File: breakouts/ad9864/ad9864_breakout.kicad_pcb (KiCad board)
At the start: 2 copper layers, 82 parts, among them P101 CONN_01X02, P102 CONN_01X08, P103 CONN_02X08, U101 CONN_SMA, U102 CONN_SMA, U103 ad9864, U104 TXCO, U105 CONN_SMA, U106 CONN_SMA, U107 max2605

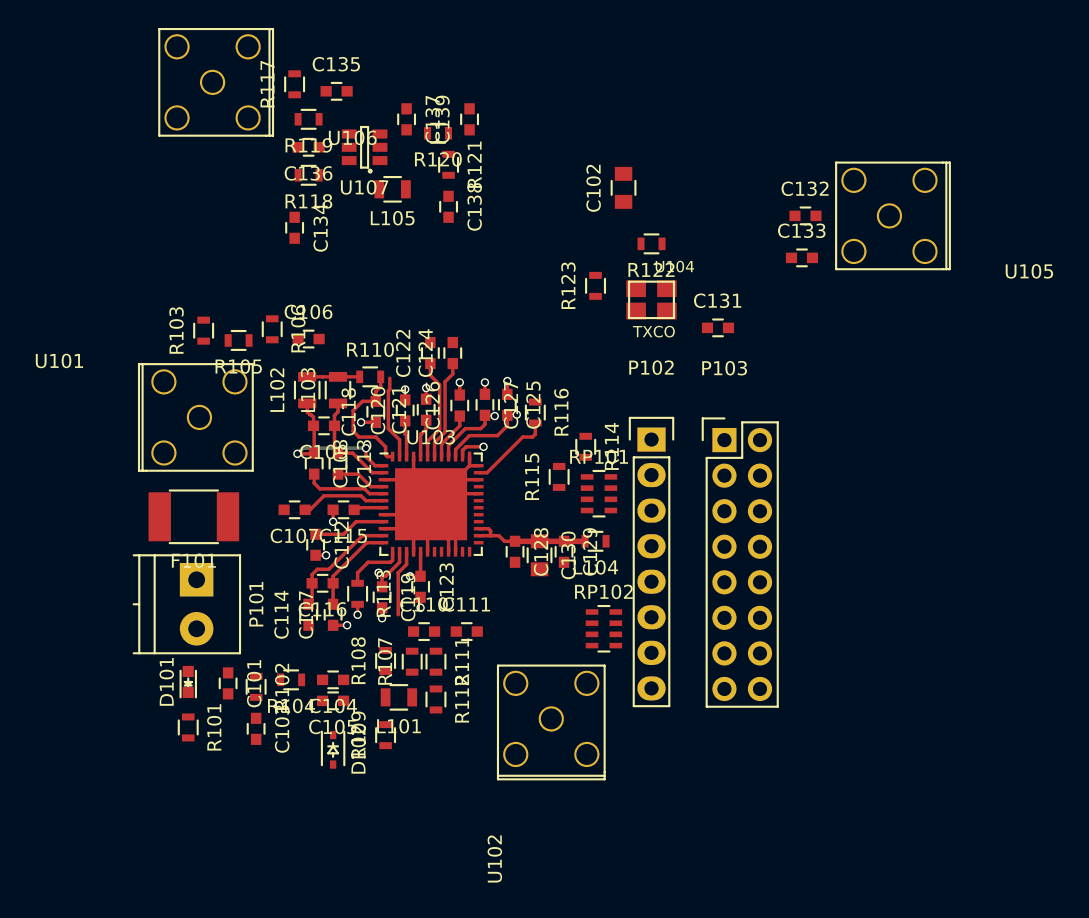
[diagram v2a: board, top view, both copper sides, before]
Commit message: finished layout of ad9864 breakout..
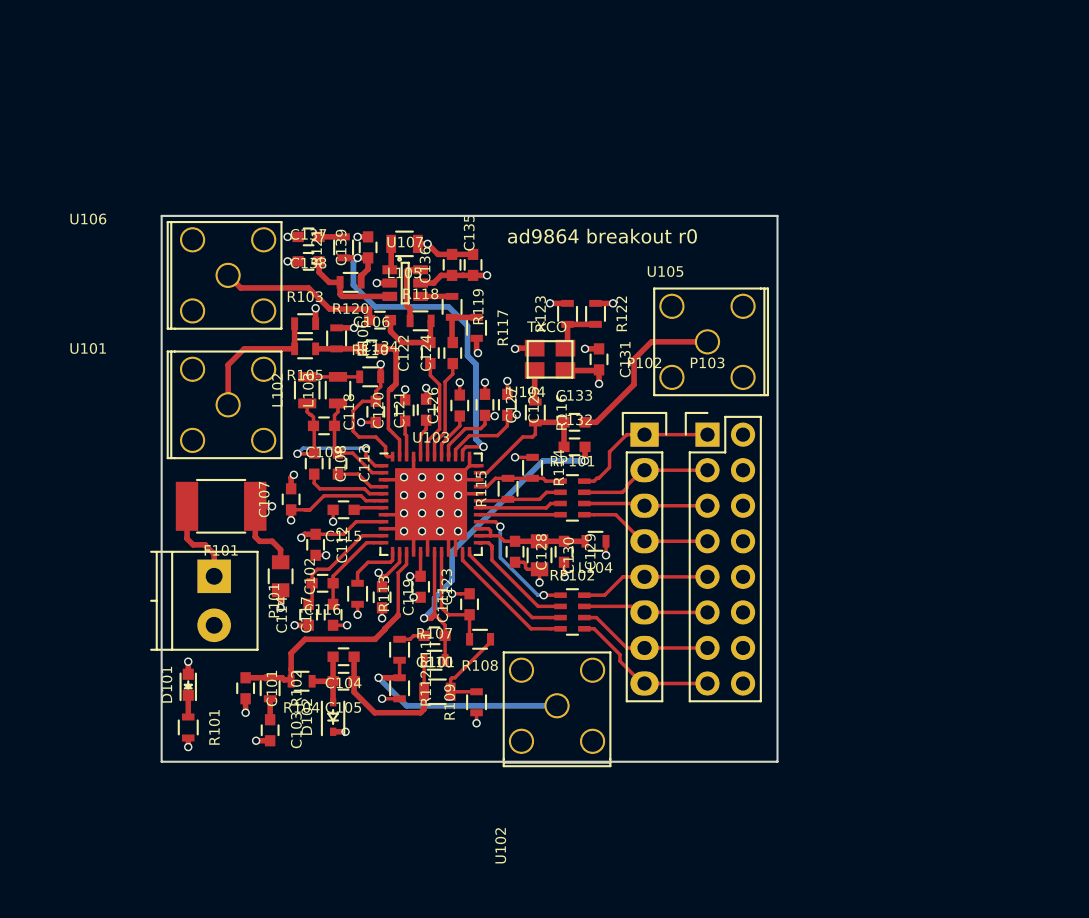
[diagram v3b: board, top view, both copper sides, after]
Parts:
- moved C102 37.0 mm to (120.5, 114.8), turned to 270 degrees
- moved C132 23.3 mm to (141.5, 105.5)
- moved R117 21.7 mm to (134.5, 97.0), turned to 270 degrees
- moved C133 20.1 mm to (141.5, 103.8)
- moved R119 16.9 mm to (132.8, 95.5), turned to 270 degrees
- moved U105 15.8 mm to (151.0, 98.0)
- moved C135 15.8 mm to (134.2, 92.5), turned to 90 degrees
- moved U106 13.8 mm to (116.8, 93.2), turned to 0 degrees
- moved C136 13.3 mm to (132.8, 92.5), turned to 90 degrees
- moved R118 13.1 mm to (130.5, 96.5), turned to 0 degrees
- moved R120 12.3 mm to (125.5, 93.8)
- moved C137 12.3 mm to (122.5, 92.2), turned to 0 degrees
- moved C139 11.7 mm to (126.8, 91.2)
- moved C138 10.2 mm to (122.5, 90.5), turned to 180 degrees
- moved U107 10.1 mm to (129.4, 93.8), turned to 0 degrees
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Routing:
- net GND: track 29.9 -> 57.8 mm, vias 12 -> 50
- net /CLKP: track 0.00 -> 27.7 mm, vias 0 -> 2
- net +3V3: track 38.6 -> 63.1 mm, vias 4 -> 15
- net /IOUTL: track 2.05 -> 26.3 mm, vias 1 -> 2
- net Net-(R111-Pad2): track 0.00 -> 16.3 mm, vias 0 -> 1
- net /IOUTC: track 4.75 -> 18.9 mm
- net Net-(C133-Pad2): track 0.00 -> 12.2 mm
- net Net-(C134-Pad2): track 0.00 -> 11.9 mm
- net Net-(C104-Pad1): track 0.00 -> 11.7 mm
- net /SYNCB: track 0.00 -> 11.0 mm
- net /PC: track 0.00 -> 10.7 mm
- net Net-(R103-Pad1): track 0.00 -> 9.88 mm
- net /FS: track 0.00 -> 9.79 mm
- net /PD: track 0.00 -> 9.70 mm
- net Net-(RP102-Pad4): track 0.00 -> 9.63 mm
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- added copper zone on In2.Cu, net +3V3
- added copper zone on In1.Cu, net GND
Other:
- board outline added: 44 x 39 mm
- copper layers 2 -> 4
- board text added: "ad9864 breakout r0"

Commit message: finished ad9864 silkscreen cleanup, ordered r0
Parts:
- moved U105 0.90 mm to (151.9, 98.0)
- moved U101 0.76 mm to (116.0, 102.4)
- moved U106 0.75 mm to (116.0, 93.2)
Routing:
- net Net-(C133-Pad2): track 12.2 -> 13.1 mm
- net Net-(C134-Pad2): track 11.9 -> 12.6 mm
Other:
- board text added: "3v3"
- board text added: "clkp"
- board text added: "fref"
- board text added: "if in"
- board text added: "lo"
- board text added: "pc pd pe ck da db fs sb"

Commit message: tested ethernet vna control
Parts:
- added U108: mounting_box, vna_footprints:momo, B.Cu at (122.5, 117.5)
